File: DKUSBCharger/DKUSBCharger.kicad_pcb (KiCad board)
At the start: 2 copper layers, 8.7 x 4.4 mm, 18 parts, among them J1 Conn_01x02, J2 10118192-0002LF, J3 USB_C_Receptacle_USB2.0_16P, J4 USB_A

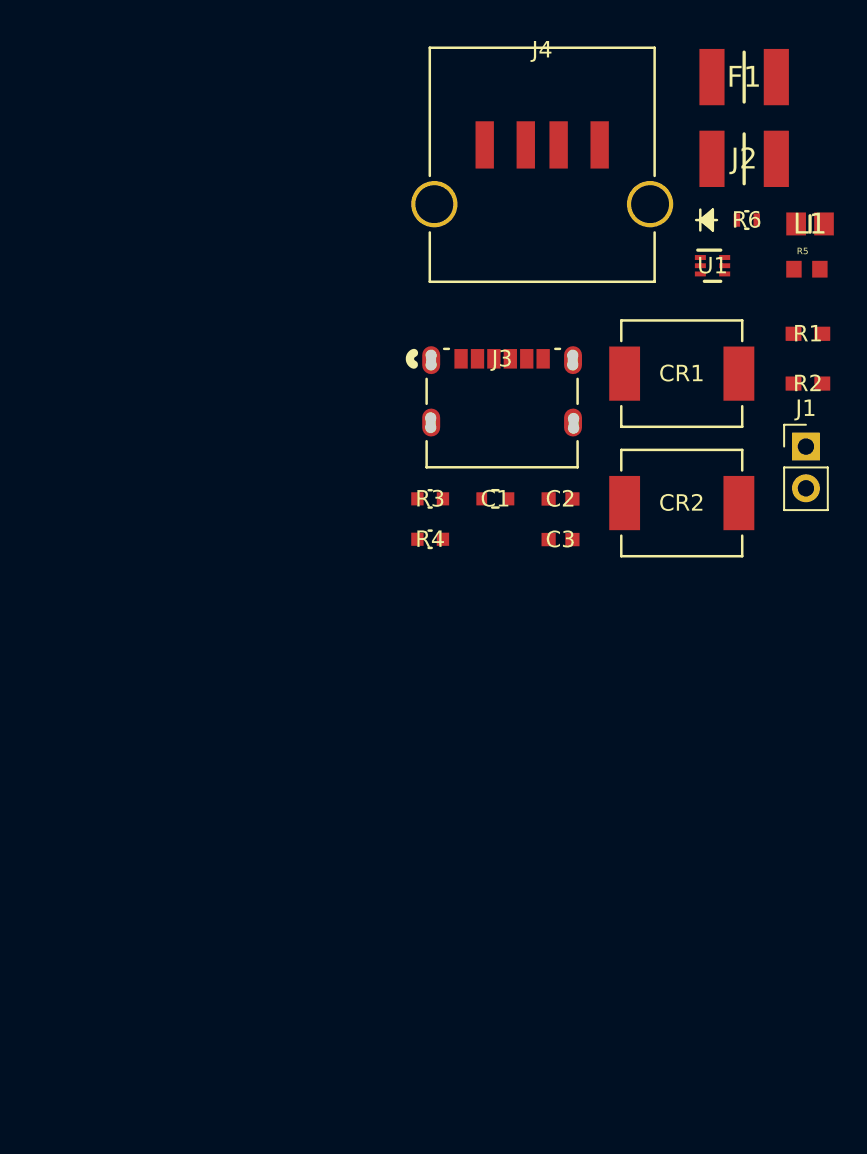
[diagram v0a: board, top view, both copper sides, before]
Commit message: Fixed footprints; started PCB floorplanning
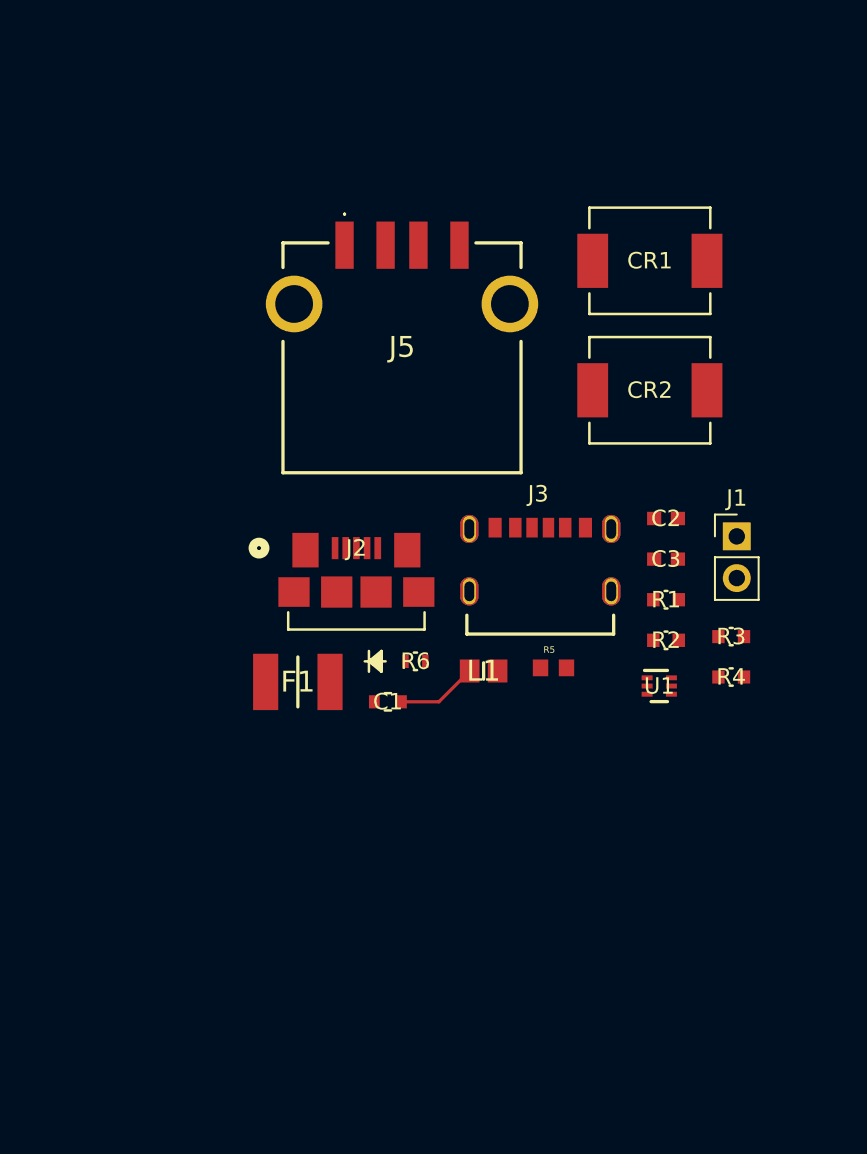
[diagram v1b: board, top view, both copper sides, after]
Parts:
- removed J4: USB_A, footprints_USB_Type_A_Receptacle:Conn_USB-87583_AMP
- added J5: 87583-2010BLF, USBChargerFootprints:875832010BLF, F.Cu at (850.7, 223.6)
- C1: footprint footprints_10uF_CAP:CAP_CL10_SAM -> USBChargerFootprints:CAP_CL10_SAM
- C2, C3: footprint footprints_22uF_CAP:G-188_MUR -> USBChargerFootprints:G-188_MUR
- CR1, CR2: footprint footprints_Schottky_60V_3A:SMCDO-214AB_MCC -> USBChargerFootprints:SMCDO-214AB_MCC
- F1: footprint footprints_fuse_2.6A_12V:FUSC4632X205N -> USBChargerFootprints:FUSC4632X205N
- J2: footprint footprints_fuse_2.6A_12V:FUSC4632X205N -> USBChargerFootprints:CONN_10118192-0002LF_AMP
- J3: value USB_C_Receptacle_USB2.0_16P -> USB4125-GF-A_REVA2; footprint footprints_USB_Type_C_Receptacle:CONN6_USB4125_GCT -> USBChargerFootprints:GCT_USB4125-GF-A_REVA2
- L1: footprint Inductor_1uF:INDC2012X80N -> USBChargerFootprints:INDC2012X80N
- R1, R2: footprint footprints_resistor_5.1k:RC0603N_YAG-M -> USBChargerFootprints:RC0603N_YAG
- R3: footprint Resistor_732k:RC0603N_PAN -> USBChargerFootprints:RC0603N_PAN
- R4: footprint footprints_resistor_100k:RC0603N_PAN -> USBChargerFootprints:RC0603N_PAN_100k
- R5: footprint RR0816P_2800_D_44A:RESC1608X50N -> USBChargerFootprints:RESC1608X50N
- R6: footprint footprints_LED_orange:LED_SMLD12_ROM -> USBChargerFootprints:LED_SMLD12_ROM
- U1: footprint footprints_regulator_boost_3A_ADJ:DRL0006A -> USBChargerFootprints:DRL0006A
- moved F1 45.8 mm to (844.3, 243.3)
- moved J2 35.1 mm to (847.9, 237.4)
- moved L1 33.7 mm to (855.6, 242.6)
- moved R6 33.6 mm to (851.5, 242.0)
- moved R5 28.8 mm to (859.9, 242.4)
- moved U1 25.8 mm to (866.3, 243.5)
- moved R3 20.2 mm to (870.7, 240.5)
- moved R4 20.2 mm to (870.7, 243.0)
- moved R1 18.4 mm to (866.8, 238.3)
- moved R2 17.9 mm to (866.8, 240.8)
- moved C1 14.0 mm to (849.8, 244.5)
- moved J3 10.6 mm to (859.1, 237.0)
- moved CR1 7.14 mm to (865.8, 217.7)
- moved CR2 7.14 mm to (865.8, 225.5)
- moved J1 6.90 mm to (871.1, 234.4)
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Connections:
- R1 pad 1: +5V -> /CC1
- R1 pad 2: /CC1 -> +5V
- R2 pad 1: +5V -> /CC2
- R2 pad 2: /CC2 -> +5V
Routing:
- net /EN: track 0.00 -> 4.93 mm
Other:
- board outline removed

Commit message: Finished PCB
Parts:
- moved J1 42.0 mm to (832.2, 218.5), turned to 90 degrees
- moved J5 36.4 mm to (840.5, 258.5), turned to 180 degrees
- moved R2 26.8 mm to (840.0, 242.5), turned to -90 degrees
- moved R1 26.8 mm to (840.0, 239.3), turned to 90 degrees
- moved J3 25.0 mm to (834.3, 240.5), turned to -90 degrees
- moved U1 24.0 mm to (843.5, 236.2), turned to -90 degrees
- moved C2 23.9 mm to (843.5, 239.0)
- moved C3 23.8 mm to (843.5, 241.0)
- moved R4 23.4 mm to (848.0, 237.5), turned to 180 degrees
- moved R3 23.3 mm to (848.0, 235.5), turned to 180 degrees
- moved CR1 20.8 mm to (845.0, 219.0), turned to 180 degrees
- moved CR2 20.8 mm to (845.0, 226.5), turned to 180 degrees
- moved J2 17.4 mm to (833.5, 227.7), turned to -90 degrees
- moved L1 16.6 mm to (841.5, 233.8), turned to -90 degrees
- moved C1 12.8 mm to (843.5, 233.3), turned to -90 degrees
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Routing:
- net +5V: track 0.00 -> 97.9 mm, vias 0 -> 2
- net Net-(CR1-Pad1): track 0.00 -> 18.0 mm
- net /FB: track 0.00 -> 8.75 mm
- net Net-(J5-Pad2): track 0.00 -> 8.28 mm
- net Net-(CR2-Pad2): track 0.00 -> 5.89 mm
- net GND: track 0.00 -> 5.33 mm, vias 0 -> 4
- net Net-(J2-Pad2): track 0.00 -> 4.82 mm
- net /EN: track 4.93 -> 8.67 mm
- net /SW: track 0.00 -> 3.45 mm
- net Net-(R5-Pad1): track 0.00 -> 3.08 mm
- net /CC2: track 0.00 -> 2.92 mm
- net /CC1: track 0.00 -> 2.64 mm
- added copper zone on B.Cu, net GND
- added copper zone on F.Cu, net GND
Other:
- board outline added: 25 x 55 mm

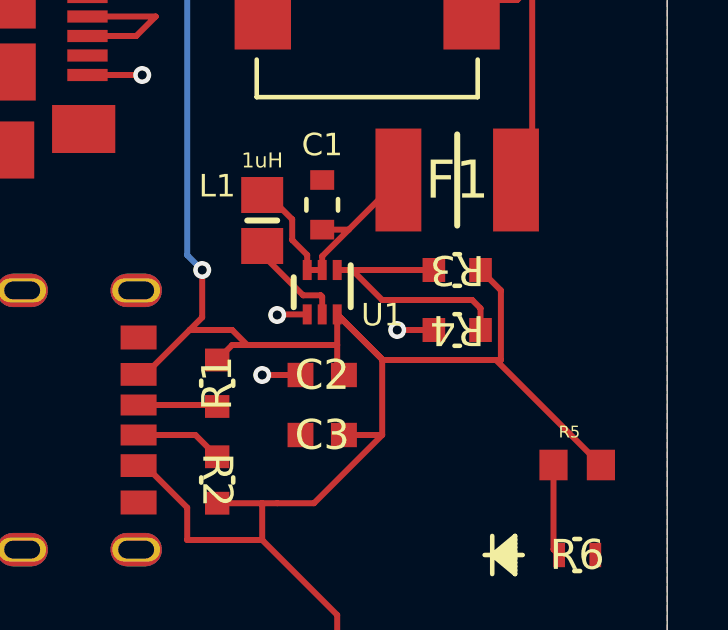
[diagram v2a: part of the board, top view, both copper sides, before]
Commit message: Fixing DRC errors
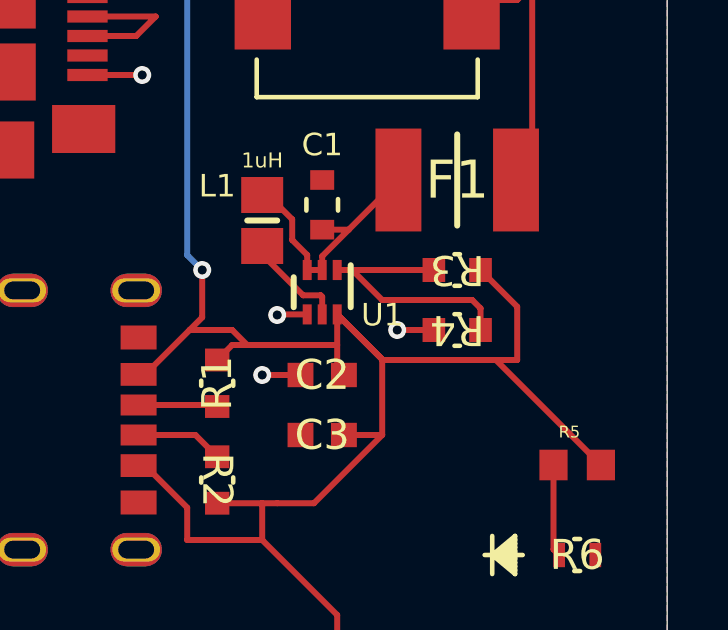
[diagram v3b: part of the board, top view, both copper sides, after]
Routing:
- net +5V: track 97.9 -> 98.7 mm
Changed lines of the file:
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@@
-	)
-	(segment
-		(start 845.519998 238.5)
-		(end 849.456598 238.5)
-		(width 0.2)
-		(layer "F.Cu")
-		(net 3)
 	)
 	(segment
@@
 	)
 	(segment
-		(start 849.456598 236.178799)
-		(end 848.777799 235.5)
-		(width 0.2)
-		(layer "F.Cu")
-		(net 3)
-	)
-	(segment
 		(start 844 238)
 		(end 844 238.7761)
@@
 	)
 	(segment
+		(start 850 236.722201)
+		(end 848.777799 235.5)
+		(width 0.2)
+		(layer "F.Cu")
+		(net 3)
+	)
+	(segment
 		(start 837.6 242.02)
 		(end 839 243.42)
@@
 	)
 	(segment
+		(start 845.519998 238.5)
+		(end 850 238.5)
+		(width 0.2)
+		(layer "F.Cu")
+		(net 3)
+	)
+	(segment
 		(start 849.29 238.5)
 		(end 852.79 242)
@@
 	)
 	(segment
+		(start 850 238.5)
+		(end 850 236.722201)
+		(width 0.2)
+		(layer "F.Cu")
+		(net 3)
+	)
+	(segment
 		(start 834.765 218.5)
 		(end 841.0202 218.5)
@@
 		(width 0.2)
 		(layer "F.Cu")
-		(net 3)
-	)
-	(segment
-		(start 849.456598 238.5)
-		(end 849.456598 236.178799)
-		(width 0.2)
-		(layer "F.Cu")

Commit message: Post check-off edits
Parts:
- moved J5 2.55 mm to (840.0, 261.0), turned to 0 degrees
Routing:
- net +5V: track 98.7 -> 87.4 mm
- net GND: track 5.33 -> 9.30 mm, vias 4 -> 6
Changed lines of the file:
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@@
 	(footprint "USBChargerFootprints:875832010BLF"
 		(layer "F.Cu")
-		(at 840.5 258.5 180)
+		(at 840 261)
 		(descr "87583-2010BLF-3")
 		(tags "Connector")
@@
 		)
 		(property "Height" "7.94"
-			(at 0 0 180)
+			(at 0 0 0)
 			(unlocked yes)
 			(layer "F.Fab")
@@
 		)
 		(property "Manufacturer_Name" "Amphenol Communications Solutions"
-			(at 0 0 180)
+			(at 0 0 0)
 			(unlocked yes)
 			(layer "F.Fab")
@@
 		)
 		(property "Manufacturer_Part_Number" "87583-2010BLF"
-			(at 0 0 180)
+			(at 0 0 0)
 			(unlocked yes)
 			(layer "F.Fab")
@@
 		)
 		(property "Mouser Part Number" ""
-			(at 0 0 180)
+			(at 0 0 0)
 			(unlocked yes)
 			(layer "F.Fab")
@@
 		)
 		(property "Mouser Price/Stock" ""
-			(at 0 0 180)
+			(at 0 0 0)
 			(unlocked yes)
 			(layer "F.Fab")
@@
 		)
 		(property "Arrow Part Number" "87583-2010BLF"
-			(at 0 0 180)
+			(at 0 0 0)
 			(unlocked yes)
 			(layer "F.Fab")
@@
 		)
 		(property "Arrow Price/Stock" "https://www.arrow.com/en/products/87583-2010blf/amphenol-fci?region=europe"
-			(at 0 0 180)
+			(at 0 0 0)
 			(unlocked yes)
 			(layer "F.Fab")
@@
 		(attr through_hole)
 		(fp_line
-			(start 7.25 7)
-			(end 7.25 -1)
+			(start -7.25 -7)
+			(end -7.25 -5.5)
 			(stroke
 				(width 0.2)
@@
 		)
 		(fp_line
-			(start 7.25 -7)
-			(end 7.25 -5.5)
+			(start -7.25 -1)
+			(end -7.25 7)
 			(stroke
 				(width 0.2)
@@
 		)
 		(fp_line
-			(start 4.5 -7)
-			(end 7.25 -7)
+			(start -7.25 7)
+			(end 7.25 7)
 			(stroke
 				(width 0.2)
@@
 		)
 		(fp_line
-			(start -3.5 -8.7)
-			(end -3.5 -8.7)
+			(start -4.5 -7)
+			(end -7.25 -7)
 			(stroke
-				(width 0.1)
+				(width 0.2)
 				(type solid)
 			)
@@
 		)
 		(fp_line
-			(start -4.5 -7)
-			(end -7.25 -7)
+			(start -3.5 -8.7)
+			(end -3.5 -8.7)
 			(stroke
-				(width 0.2)
+				(width 0.1)
 				(type solid)
 			)
@@
 		)
 		(fp_line
-			(start -7.25 7)
-			(end 7.25 7)
+			(start 4.5 -7)
+			(end 7.25 -7)
 			(stroke
 				(width 0.2)
@@
 		)
 		(fp_line
-			(start -7.25 -1)
-			(end -7.25 7)
+			(start 7.25 -7)
+			(end 7.25 -5.5)
 			(stroke
 				(width 0.2)
@@
 		)
 		(fp_line
-			(start -7.25 -7)
-			(end -7.25 -5.5)
+			(start 7.25 7)
+			(end 7.25 -1)
 			(stroke
 				(width 0.2)
@@
 		)
 		(fp_arc
-			(start -3.5 -8.7)
-			(mid -3.55 -8.75)
-			(end -3.5 -8.8)
+			(start -3.5 -8.8)
+			(mid -3.45 -8.75)
+			(end -3.5 -8.7)
 			(stroke
 				(width 0.1)
@@
 		)
 		(fp_arc
-			(start -3.5 -8.8)
-			(mid -3.45 -8.75)
-			(end -3.5 -8.7)
+			(start -3.5 -8.7)
+			(mid -3.55 -8.75)
+			(end -3.5 -8.8)
 			(stroke
 				(width 0.1)
@@
 		)
 		(fp_line
-			(start 9.295 8)
-			(end -9.295 8)
+			(start -9.295 -9.3)
+			(end 9.295 -9.3)
 			(stroke
 				(width 0.1)
@@
 		)
 		(fp_line
-			(start 9.295 -9.3)
-			(end 9.295 8)
+			(start -9.295 8)
+			(end -9.295 -9.3)
 			(stroke
 				(width 0.1)
@@
 		)
 		(fp_line
-			(start -9.295 8)
-			(end -9.295 -9.3)
+			(start 9.295 -9.3)
+			(end 9.295 8)
 			(stroke
 				(width 0.1)
@@
 		)
 		(fp_line
-			(start -9.295 -9.3)
-			(end 9.295 -9.3)
+			(start 9.295 8)
+			(end -9.295 8)
 			(stroke
 				(width 0.1)
@@
 		)
 		(fp_line
-			(start 7.25 7)
-			(end -7.25 7)
+			(start -7.25 -7)
+			(end 7.25 -7)
 			(stroke
 				(width 0.1)
@@
 		)
 		(fp_line
-			(start 7.25 -7)
-			(end 7.25 7)
+			(start -7.25 7)
+			(end -7.25 -7)
 			(stroke
 				(width 0.1)
@@
 		)
 		(fp_line
-			(start -7.25 7)
-			(end -7.25 -7)
+			(start 7.25 -7)
+			(end 7.25 7)
 			(stroke
 				(width 0.1)
@@
 		)
 		(fp_line
-			(start -7.25 -7)
-			(end 7.25 -7)
+			(start 7.25 7)
+			(end -7.25 7)
 			(stroke
 				(width 0.1)
@@
 		)
 		(pad "1" smd rect
-			(at -3.5 -6.86 180)
+			(at -3.5 -6.86)
 			(size 1.12 2.88)
 			(layers "F.Cu" "F.Mask" "F.Paste")
@@
 		)
 		(pad "2" smd rect
-			(at -1 -6.86 180)
+			(at -1 -6.86)
 			(size 1.12 2.88)
 			(layers "F.Cu" "F.Mask" "F.Paste")
@@
 		)
 		(pad "3" smd rect
-			(at 1 -6.86 180)
+			(at 1 -6.86)
 			(size 1.12 2.88)
 			(layers "F.Cu" "F.Mask" "F.Paste")
@@
 		)
 		(pad "4" smd rect
-			(at 3.5 -6.86 180)
+			(at 3.5 -6.86)
 			(size 1.12 2.88)
 			(layers "F.Cu" "F.Mask" "F.Paste")
@@
 		)
 		(pad "MH1" thru_hole circle
-			(at -6.57 -3.28 180)
+			(at -6.57 -3.28)
 			(size 3.45 3.45)
 			(drill 2.3)
@@
 		)
 		(pad "MH2" thru_hole circle
-			(at 6.57 -3.28 180)
+			(at 6.57 -3.28)
 			(size 3.45 3.45)
 			(drill 2.3)
@@
 	)
 	(segment
+		(start 837.38 243.25)
+		(end 835.75 243.25)
+		(width 0.2)
+		(layer "F.Cu")
+		(net 2)
+	)
+	(segment
 		(start 835.675001 229)
 		(end 837.5 229)
@@
 		(net 2)
 	)
+	(segment
+		(start 835.75 237.75)
+		(end 835.5 238)
+		(width 0.2)
+		(layer "F.Cu")
+		(net 2)
+	)
+	(segment
+		(start 837.38 237.75)
+		(end 835.75 237.75)
+		(width 0.2)
+		(layer "F.Cu")
+		(net 2)
+	)
+	(segment
+		(start 835.75 243.25)
+		(end 835.5 243)
+		(width 0.2)
+		(layer "F.Cu")
+		(net 2)
+	)
 	(via
 		(at 842 237)
@@
 	)
 	(via
+		(at 835.5 238)
+		(size 0.6)
+		(drill 0.3)
+		(layers "F.Cu" "B.Cu")
+		(free yes)
+		(net 2)
+	)
+	(via
+		(at 835.5 243)
+		(size 0.6)
+		(drill 0.3)
+		(layers "F.Cu" "B.Cu")
+		(free yes)
+		(net 2)
+	)
+	(via
 		(at 846 237.5)
 		(size 0.6)
@@
 	)
 	(segment
+		(start 839 250)
+		(end 836.5 252.5)
+		(width 0.2)
+		(layer "F.Cu")
+		(net 3)
+	)
+	(segment
 		(start 845.5 238.480002)
 		(end 845.5 241)
@@
 	)
 	(segment
+		(start 839 244.5)
+		(end 839 250)
+		(width 0.2)
+		(layer "F.Cu")
+		(net 3)
+	)
+	(segment
 		(start 840 238.5)
 		(end 840.5 238)
@@
 	)
 	(segment
-		(start 844 247)
-		(end 844 265.36)
+		(start 836.5 252.5)
+		(end 836.5 254.14)
 		(width 0.2)
 		(layer "F.Cu")
@@
 	)
 	(segment
-		(start 841.5 244.5)
-		(end 844 247)
-		(width 0.2)
-		(layer "F.Cu")
-		(net 3)
-	)
-	(segment
 		(start 843.2253 243.2747)
 		(end 845.5 241)
@@
 	)
 	(segment
-		(start 841.5 265.36)
-		(end 841.5 268.5)
+		(start 839 254.14)
+		(end 839 251)
 		(width 0.2)
 		(layer "F.Cu")
@@
 	)
 	(segment
-		(start 841.5 268.5)
-		(end 839.5 268.5)
+		(start 839 251)
+		(end 841 251)
 		(width 0.2)
 		(layer "F.Cu")
@@
 	)
 	(segment
-		(start 839.5 268.5)
-		(end 839.5 265.36)
+		(start 841 251)
+		(end 841 254.14)
 		(width 0.2)
 		(layer "F.Cu")
